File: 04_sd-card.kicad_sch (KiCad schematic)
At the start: 14 parts, among them J1 Micro_SD_Card_Det2

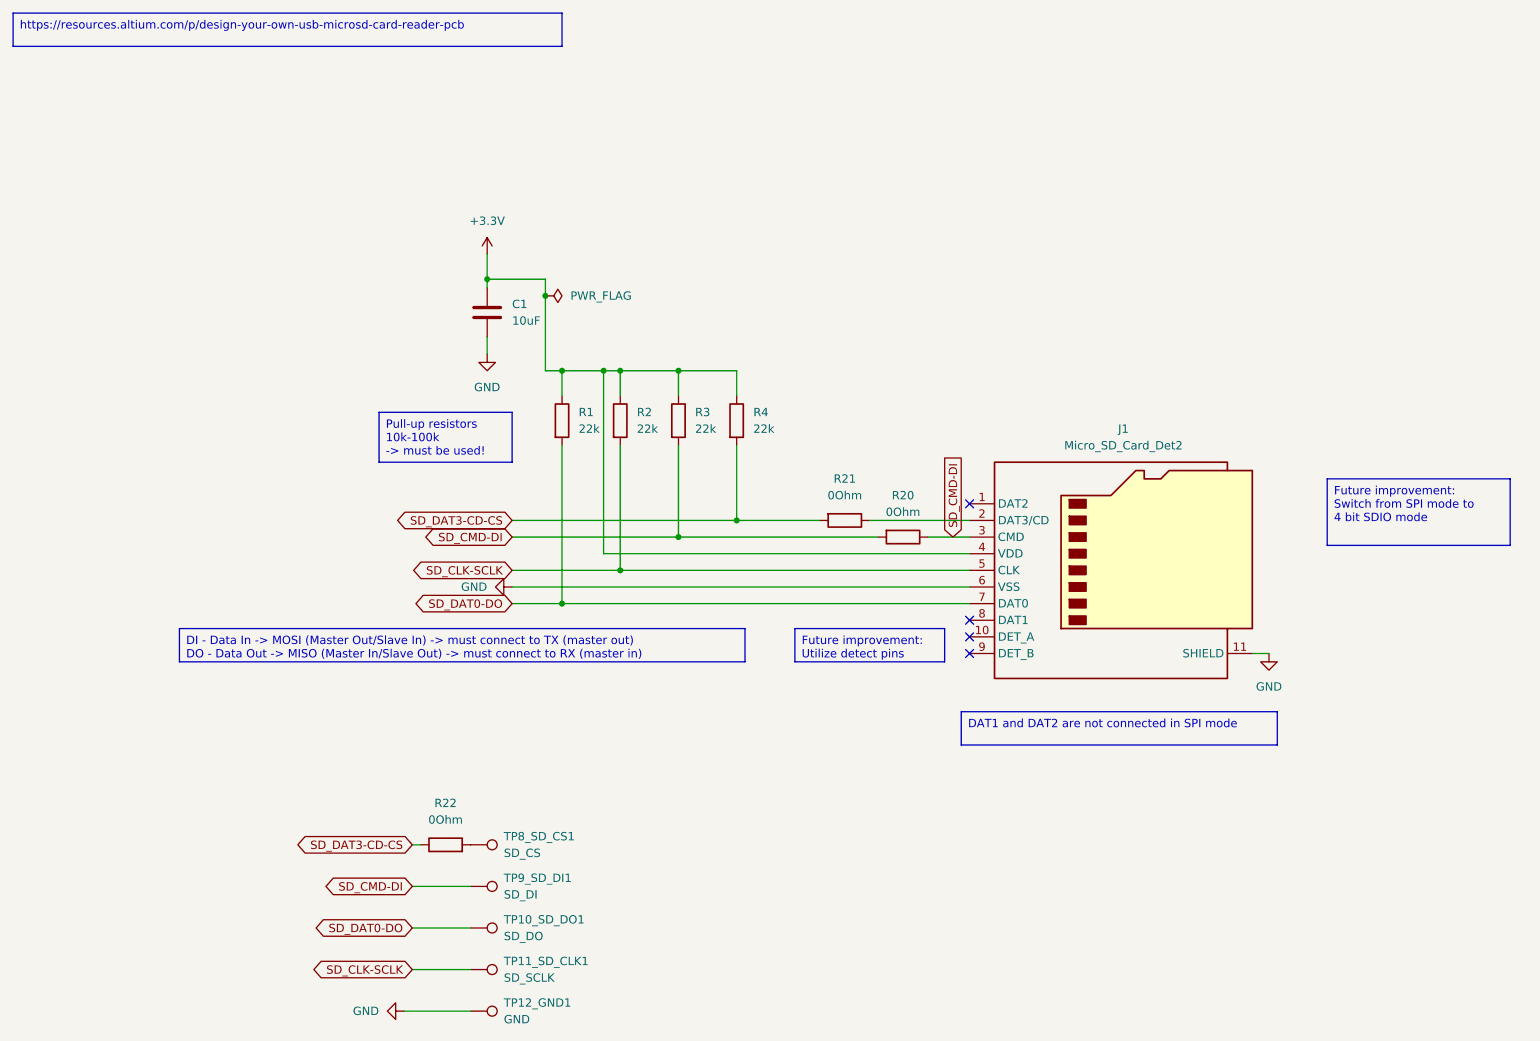
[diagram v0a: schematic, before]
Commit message: Migrate to KiCad 9, start working on the new revision
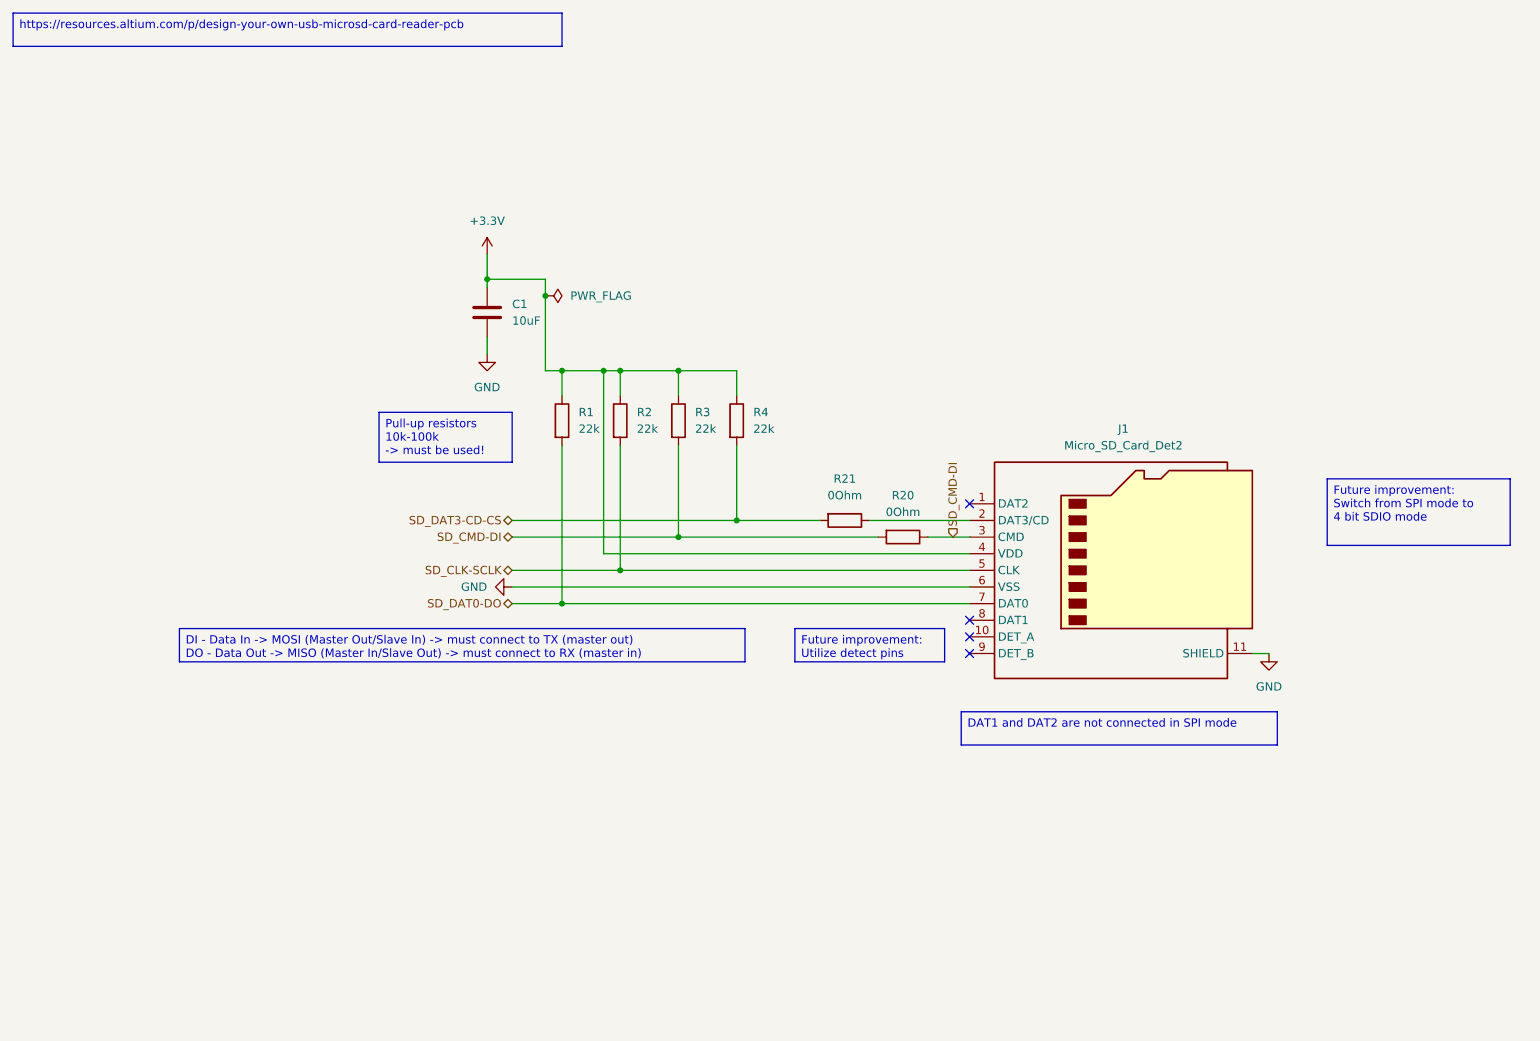
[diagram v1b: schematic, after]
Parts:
- removed R22: 0Ohm, Resistor_SMD:R_1206_3216Metric_Pad1.30x1.75mm_HandSolder, symbol Device:R
- removed TP10_SD_DO1: SD_DO, TestPoint:TestPoint_Plated_Hole_D2.0mm, symbol Connector:TestPoint
- removed TP11_SD_CLK1: SD_SCLK, TestPoint:TestPoint_Plated_Hole_D2.0mm, symbol Connector:TestPoint
- removed TP12_GND1: GND, TestPoint:TestPoint_Plated_Hole_D2.0mm, symbol Connector:TestPoint
- removed TP8_SD_CS1: SD_CS, TestPoint:TestPoint_Plated_Hole_D2.0mm, symbol Connector:TestPoint
- removed TP9_SD_DI1: SD_DI, TestPoint:TestPoint_Plated_Hole_D2.0mm, symbol Connector:TestPoint

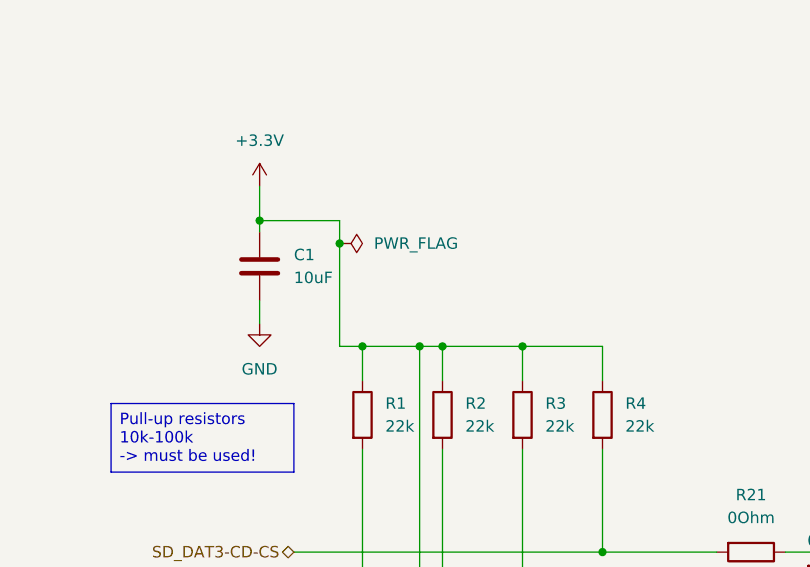
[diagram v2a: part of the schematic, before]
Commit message: switch to KiCad Pico extended symbol
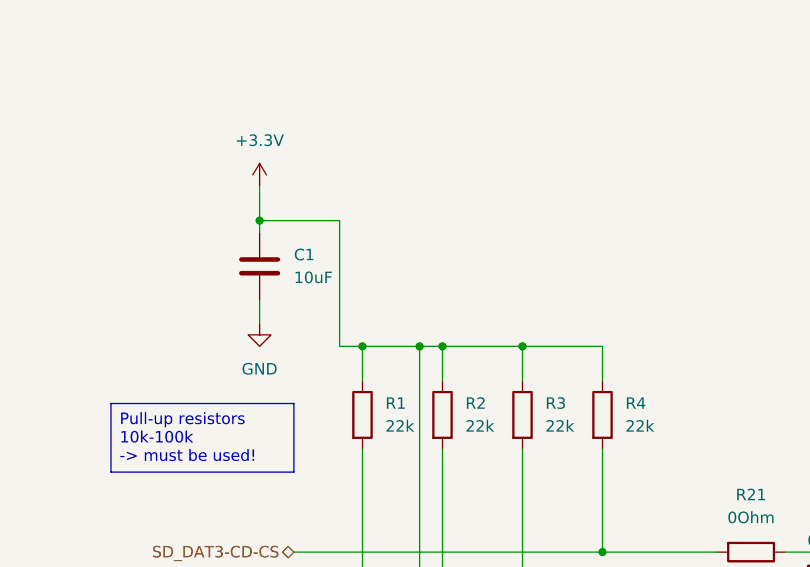
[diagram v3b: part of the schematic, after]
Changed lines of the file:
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@@
-		(color 0 0 0 0)
-	)
-	(junction
-		(at 93.98 55.88)
-		(diameter 0)
 		(color 0 0 0 0)
 	)
@@
 	(wire
 		(pts
-			(xy 93.98 55.88) (xy 93.98 67.31)
+			(xy 93.98 53.34) (xy 93.98 67.31)
 		)
 		(stroke
@@
 		(pts
 			(xy 96.52 67.31) (xy 102.87 67.31)
-		)
-		(stroke
-			(width 0)
-			(type default)
-		)
-	)
-	(wire
-		(pts
-			(xy 93.98 53.34) (xy 93.98 55.88)
 		)
 		(stroke
@@
 			)
 		)
-	)
-	(symbol
-		(lib_id "power:PWR_FLAG")
-		(at 93.98 55.88 270)
-		(unit 1)
-		(exclude_from_sim no)
-		(in_bom yes)
-		(on_board yes)
-		(dnp no)
-		(fields_autoplaced yes)
-		(property "Reference" "#FLG05"
-			(at 95.885 55.88 0)
-			(effects
-				(font
-					(size 1.27 1.27)
-				)
-				(hide yes)
-			)
-		)
-		(property "Value" "PWR_FLAG"
-			(at 97.79 55.8799 90)
-			(effects
-				(font
-					(size 1.27 1.27)
-				)
-				(justify left)
-			)
-		)
-		(property "Footprint" ""
-			(at 93.98 55.88 0)
-			(effects
-				(font
-					(size 1.27 1.27)
-				)
-				(hide yes)
-			)
-		)
-		(property "Datasheet" "~"
-			(at 93.98 55.88 0)
-			(effects
-				(font
-					(size 1.27 1.27)
-				)
-				(hide yes)
-			)
-		)
-		(property "Description" "Special symbol for telling ERC where power comes from"
-			(at 93.98 55.88 0)
-			(effects
-				(font
-					(size 1.27 1.27)
-				)
-				(hide yes)
-			)
-		)
-		(pin "1"
-		)
-		(instances
-			(project ""
-				(path "/ec954637-2a8b-4662-b4a1-f88107f11cb0/5fd074b7-3c47-4717-bcdc-b0d8134ff74e"
-					(reference "#FLG05")
-					(unit 1)
-				)
-			)
-		)

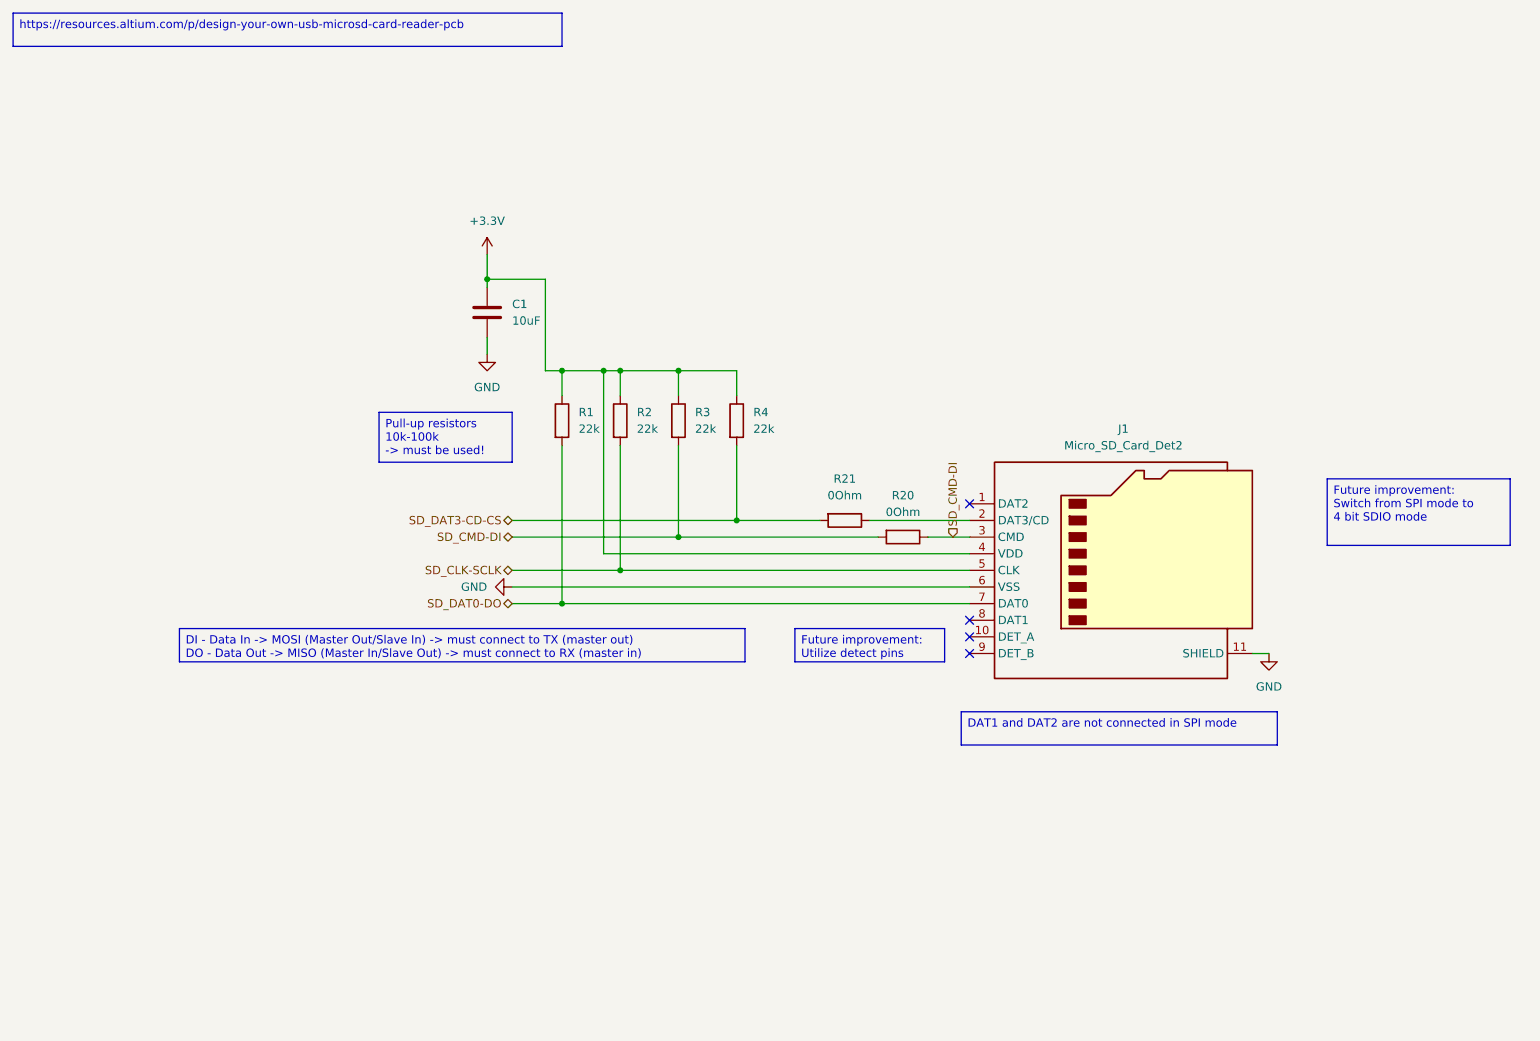
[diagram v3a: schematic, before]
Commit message: fully connect the sd connector, redraw sd and buttons
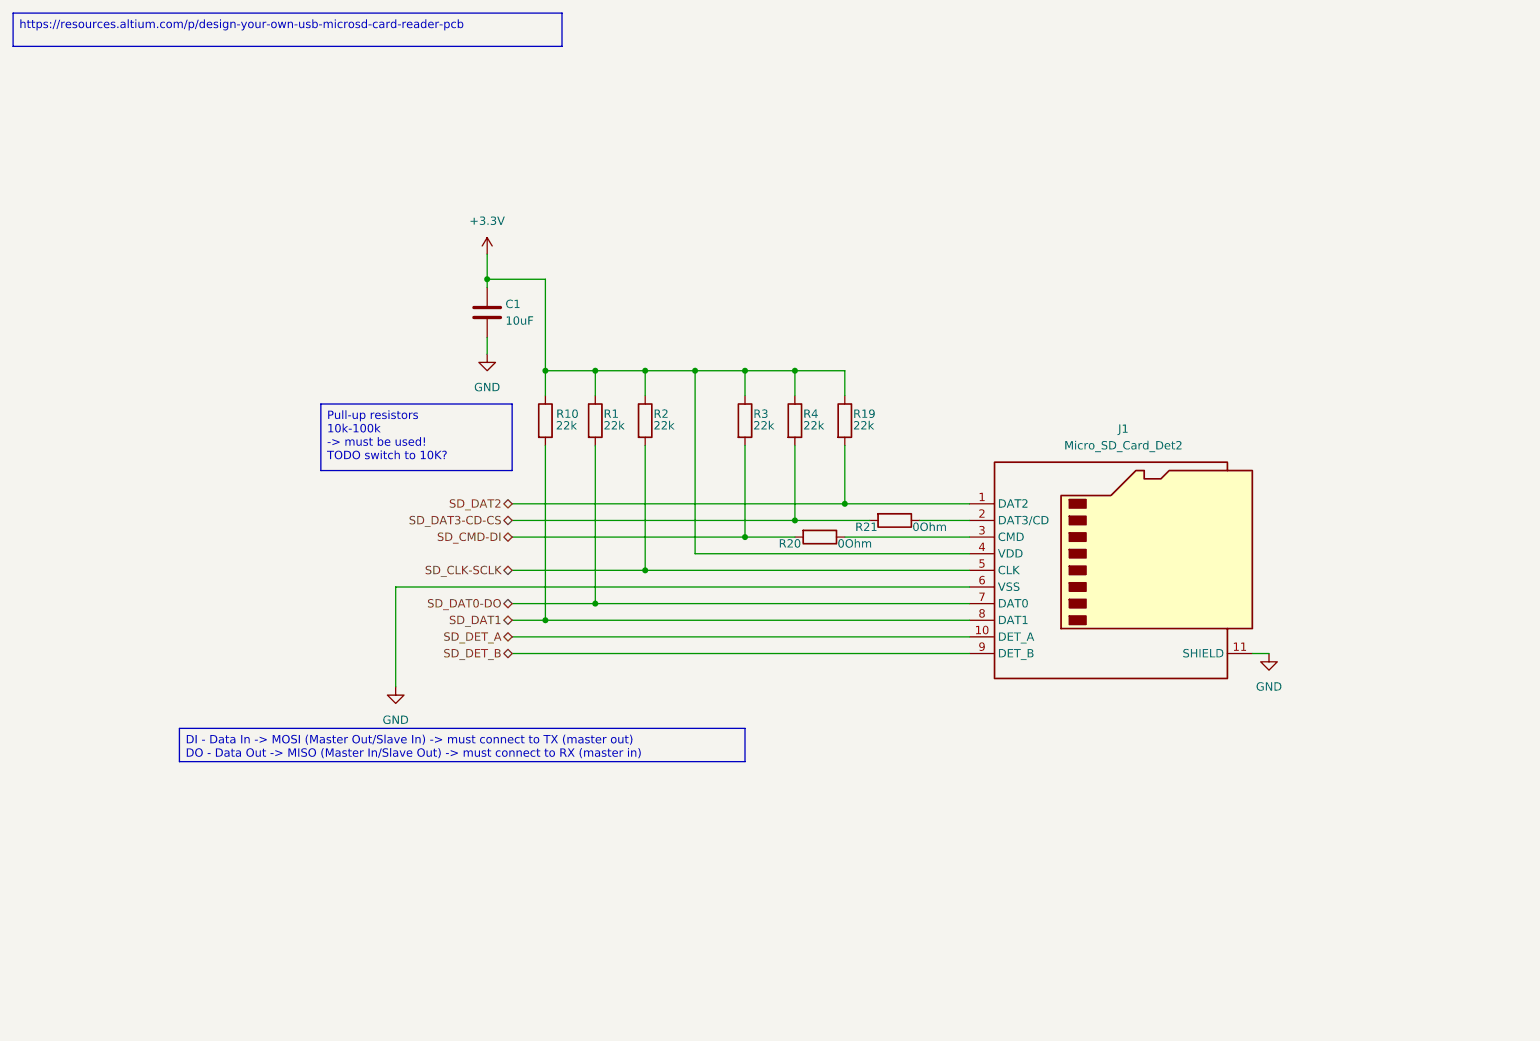
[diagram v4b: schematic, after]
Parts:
- added R10, R19: 22k, Resistor_SMD:R_1206_3216Metric_Pad1.30x1.75mm_HandSolder, symbol Device:R
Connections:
- net +3.3V: now also R10.1, R19.1
- net SD_CMD-DI: no longer J1.3 (CMD), R20.1
- net SD_DAT2: now reaches J1.1 (DAT2)
- net SD_DAT2: now also R19.2
- net SD_DET_A: now reaches J1.10 (DET_A)
- net SD_DAT1: now reaches J1.8 (DAT1)
- net SD_DAT1: now also R10.2
- net SD_DET_B: now reaches J1.9 (DET_B)
- new net: J1.3 (CMD), R20.1
- no-connect marks 4 -> 0
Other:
- moved on the sheet: R1, R2, R20, R21, R3, R4
